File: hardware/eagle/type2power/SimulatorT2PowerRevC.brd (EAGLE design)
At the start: 99.1 x 99.1 mm, 36 parts

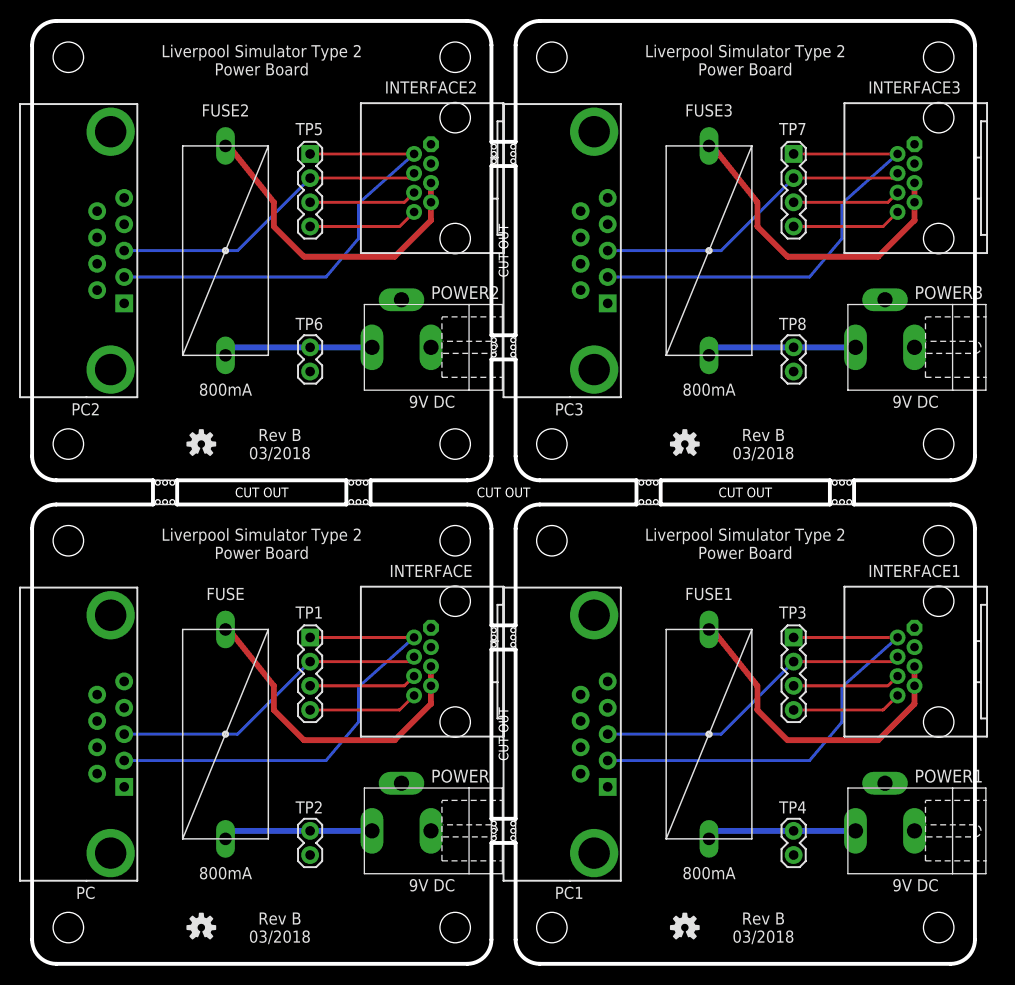
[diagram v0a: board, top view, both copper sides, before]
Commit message: Power Board Rev C
Add an indication of power supply polarity to the top silkscreen.
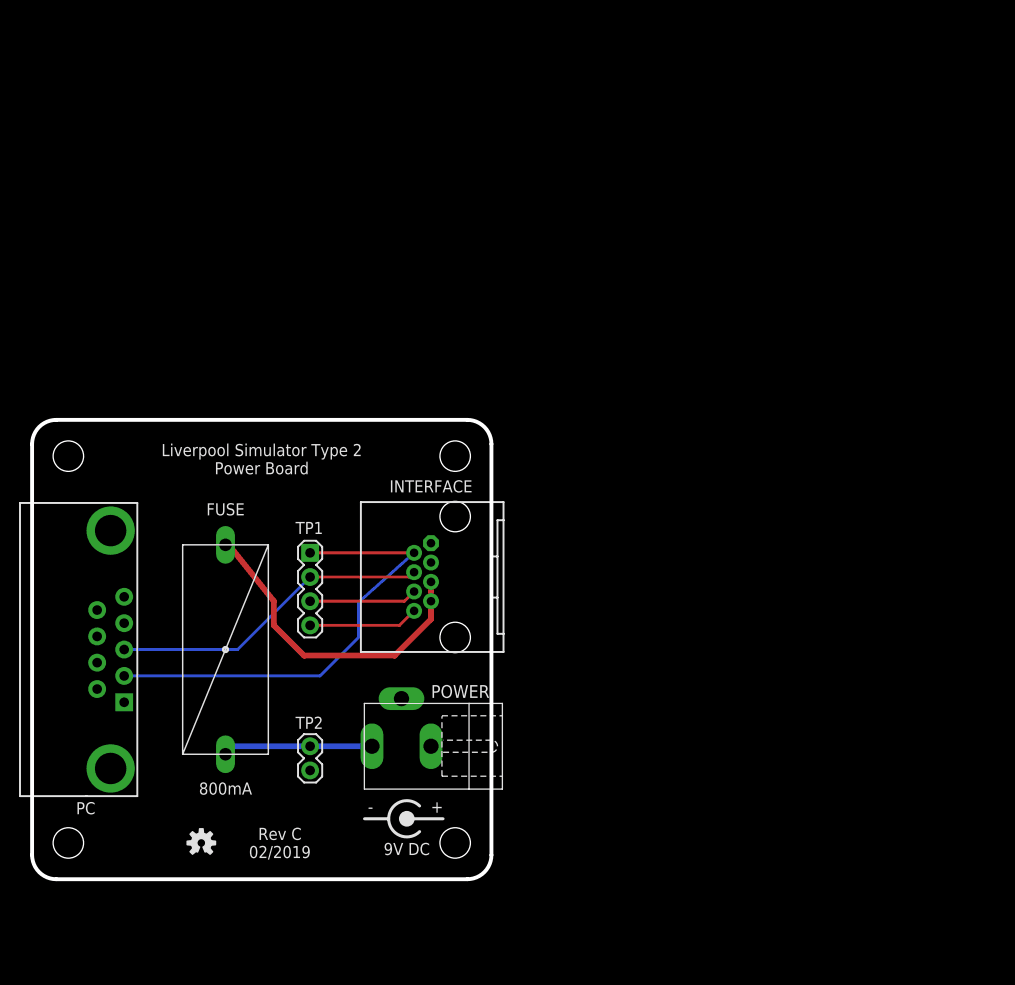
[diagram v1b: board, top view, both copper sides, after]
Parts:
- removed E$1, E$2, E$3, E$4, E$5, E$6, E$7, E$8: (no value), AIC_Custom:STAMP_HOLES
- removed FUSE1, FUSE2, FUSE3: 800mA, AIC_Custom:MCOMP-FUSE-HOLDER-PCB
- removed INTERFACE1, INTERFACE2, INTERFACE3: RJ45-RJHSE-X08090DEG, AIC_Custom:RJ45-RJHSE-5080
- removed LOGO2, LOGO3, LOGO4: OSHW-LOGOS, SparkFun-Aesthetics:OSHW-LOGO-S
- removed PC1, PC2, PC3: (no value), AIC_Custom:MULTICOMP-DB9-FEMALE-PCB-90DEG
- removed POWER1, POWER2, POWER3: 9V DC, AIC_Custom:CLIFF-FC681465P-DC-JACK
- removed TP3, TP5, TP7: (no value), SparkFun-Connectors:1X04
- removed TP4, TP6, TP8: (no value), SparkFun-Connectors:1X02
- added U$1: (no value), AIC_Custom:CENTRE-POS-SILK
- moved INTERFACE 8.89 mm to (44.5, 31.8)
- moved LOGO1 8.89 mm to (17.8, 3.81)
- moved POWER 8.89 mm to (41.9, 14.0)
- moved TP1 8.89 mm to (29.2, 34.3)
- moved TP2 8.89 mm to (29.2, 14.0)
- moved FUSE 8.89 mm to (20.3, 24.1)
- moved PC 8.89 mm to (-1.27, 24.1)
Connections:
- net P6 renamed TX2
- removed net GND1: INTERFACE1.1, INTERFACE1.3, PC1.5, POWER1.3, TP4.2
- removed net GND2: INTERFACE2.1, INTERFACE2.3, PC2.5, POWER2.3, TP6.2
- removed net GND3: INTERFACE3.1, INTERFACE3.3, PC3.5, POWER3.3, TP8.2
- removed net P1: INTERFACE1.6, TP3.3
- removed net P2: INTERFACE1.8, TP3.4
- removed net P3: INTERFACE2.6, TP5.3
- removed net P4: INTERFACE2.8, TP5.4
- removed net P5: INTERFACE3.6, TP7.3
- removed net P7: INTERFACE3.8, TP7.4
- removed net RXD1: INTERFACE1.4, PC1.3, TP3.2
- removed net RXD2: INTERFACE2.4, PC2.3, TP5.2
- removed net RXD3: INTERFACE3.4, PC3.3, TP7.2
- removed net TXD1: INTERFACE1.2, PC1.2, TP3.1
- removed net TXD2: INTERFACE2.2, PC2.2, TP5.1
- removed net TXD3: INTERFACE3.2, PC3.2, TP7.1
- removed net VIN1: FUSE1.2, POWER1.1, TP4.1
- removed net VIN3: FUSE1.1, INTERFACE1.5, INTERFACE1.7
- removed net VIN4: FUSE2.2, POWER2.1, TP6.1
- removed net VIN5: FUSE2.1, INTERFACE2.5, INTERFACE2.7
- removed net VIN6: FUSE3.2, POWER3.1, TP8.1
- removed net VIN7: FUSE3.1, INTERFACE3.5, INTERFACE3.7
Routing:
- net TXD3: track 48.9 -> 0.00 mm
- net TXD1: track 48.9 -> 0.00 mm
- net TXD2: track 48.9 -> 0.00 mm
- net VIN7: track 34.4 -> 0.00 mm
- net VIN5: track 34.4 -> 0.00 mm
- net VIN3: track 34.4 -> 0.00 mm
- net RXD3: track 33.8 -> 0.00 mm
- net RXD2: track 33.8 -> 0.00 mm
- net RXD1: track 33.8 -> 0.00 mm
- net VIN6: track 15.9 -> 0.00 mm
- net VIN4: track 15.9 -> 0.00 mm
- net VIN1: track 15.9 -> 0.00 mm
- net P7: track 11.6 -> 0.00 mm
- net P4: track 11.6 -> 0.00 mm
- net P2: track 11.6 -> 0.00 mm
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- removed copper zone on layer 1, net GND1
- removed copper zone on layer 16, net GND1
- removed copper zone on layer 1, net GND2
- removed copper zone on layer 16, net GND2
- removed copper zone on layer 1, net GND3
- removed copper zone on layer 16, net GND3
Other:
- board size 99.1 x 99.1 mm -> 48.3 x 48.3 mm
- board text added: "Rev C 02/2019"
- board text removed: "CUT OUT"
- board text removed: "FUSE"
- board text removed: "INTERFACE"
- board text removed: "PC"
- board text removed: "POWER"
- board text removed: "Rev B 03/2018"
- board text removed: "TP1"
- board text removed: "TP2"
